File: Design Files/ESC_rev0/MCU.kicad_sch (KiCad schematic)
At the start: 35 parts, among them J1 Conn_01x08, J2 Conn_01x06, J3 Conn_01x03, SW1 Push Button, U4 STM32F405RGTx, Y1 Crystal

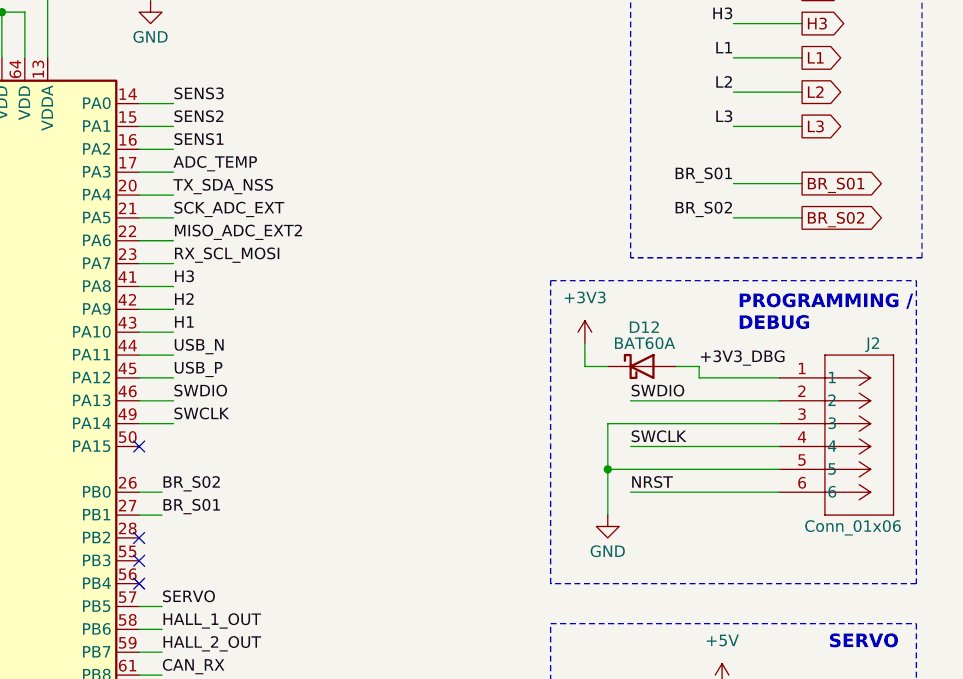
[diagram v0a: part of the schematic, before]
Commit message: update 18
Route process partially complete. Some corrections were made in footprints and pins references. Probably the power lines will need changes in size.
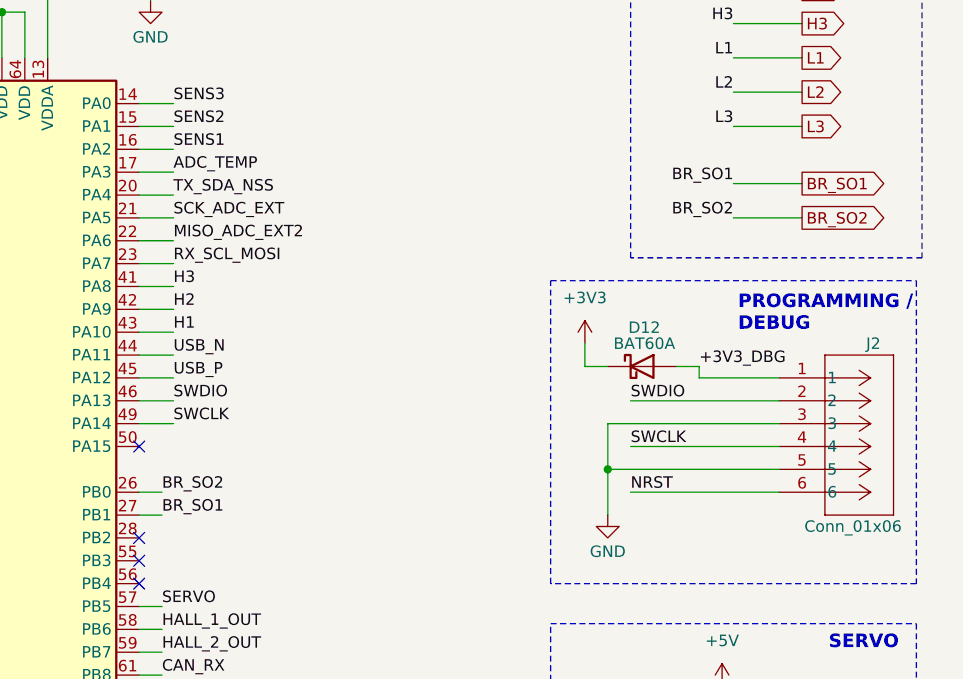
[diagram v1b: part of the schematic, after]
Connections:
- net BR_S01 renamed BR_SO1
- net BR_S02 renamed BR_SO2
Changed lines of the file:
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@@
 		)
 	)
-	(label "BR_S02"
+	(label "BR_SO2"
 		(at 182.88 115.57 0)
 		(fields_autoplaced yes)
@@
 		)
 	)
-	(label "BR_S01"
+	(label "BR_SO1"
 		(at 182.88 118.11 0)
 		(fields_autoplaced yes)
@@
 		)
 	)
-	(label "BR_S01"
+	(label "BR_SO1"
 		(at 246.38 81.28 180)
 		(fields_autoplaced yes)
@@
 		)
 	)
-	(label "BR_S02"
+	(label "BR_SO2"
 		(at 246.38 85.09 180)
 		(fields_autoplaced yes)
@@
 		)
 	)
-	(global_label "BR_S01"
+	(global_label "BR_SO1"
 		(shape output)
 		(at 254 81.28 0)
@@
 		)
 		(property "Intersheetrefs" "${INTERSHEET_REFS}"
-			(at 264.1213 81.28 0)
+			(at 264.2423 81.28 0)
 			(effects
 				(font
@@
 		)
 	)
-	(global_label "BR_S02"
+	(global_label "BR_SO2"
 		(shape output)
 		(at 254 85.09 0)
@@
 		)
 		(property "Intersheetrefs" "${INTERSHEET_REFS}"
-			(at 264.1213 85.09 0)
+			(at 264.2423 85.09 0)
 			(effects
 				(font
@@
 		(on_board yes)
 		(dnp no)
-		(fields_autoplaced yes)
 		(property "Reference" "FB1"
 			(at 191.7192 38.1 90)

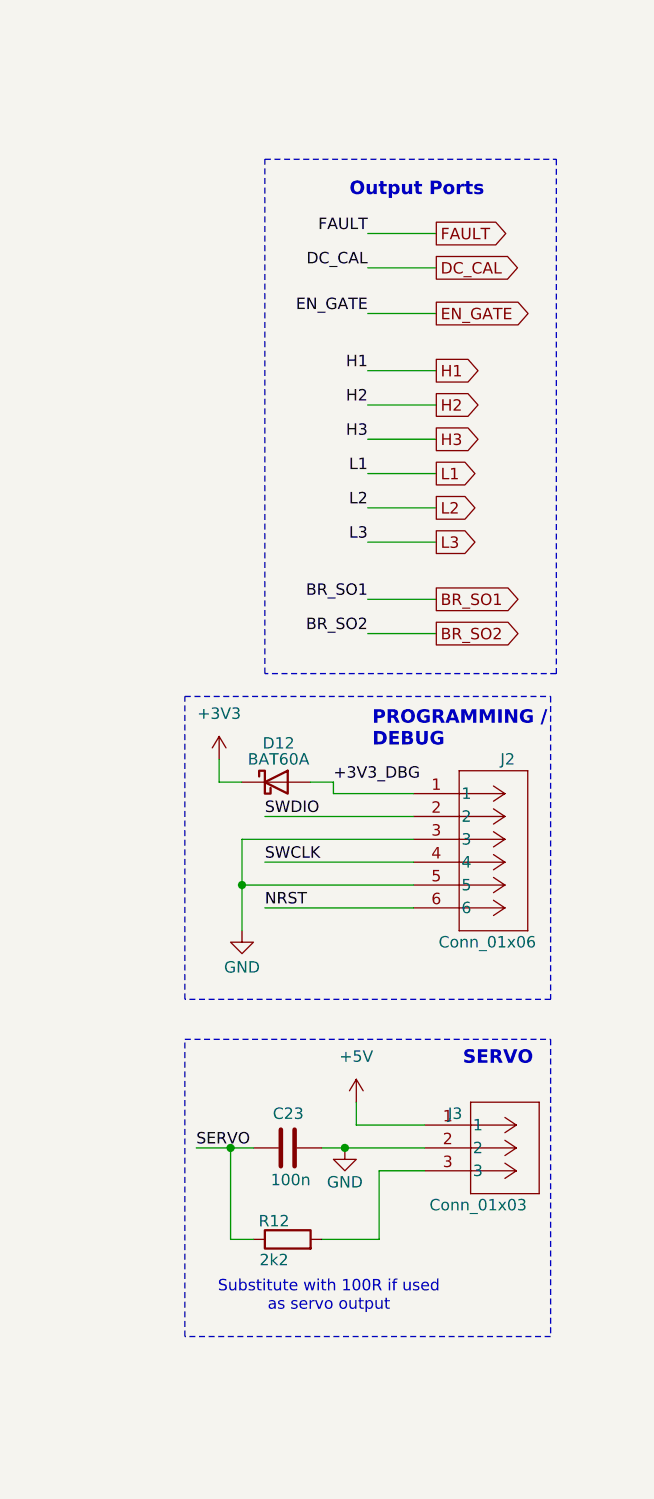
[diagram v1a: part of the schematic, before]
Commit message: update 19
Preliminary routing finished, all signaling connections made.
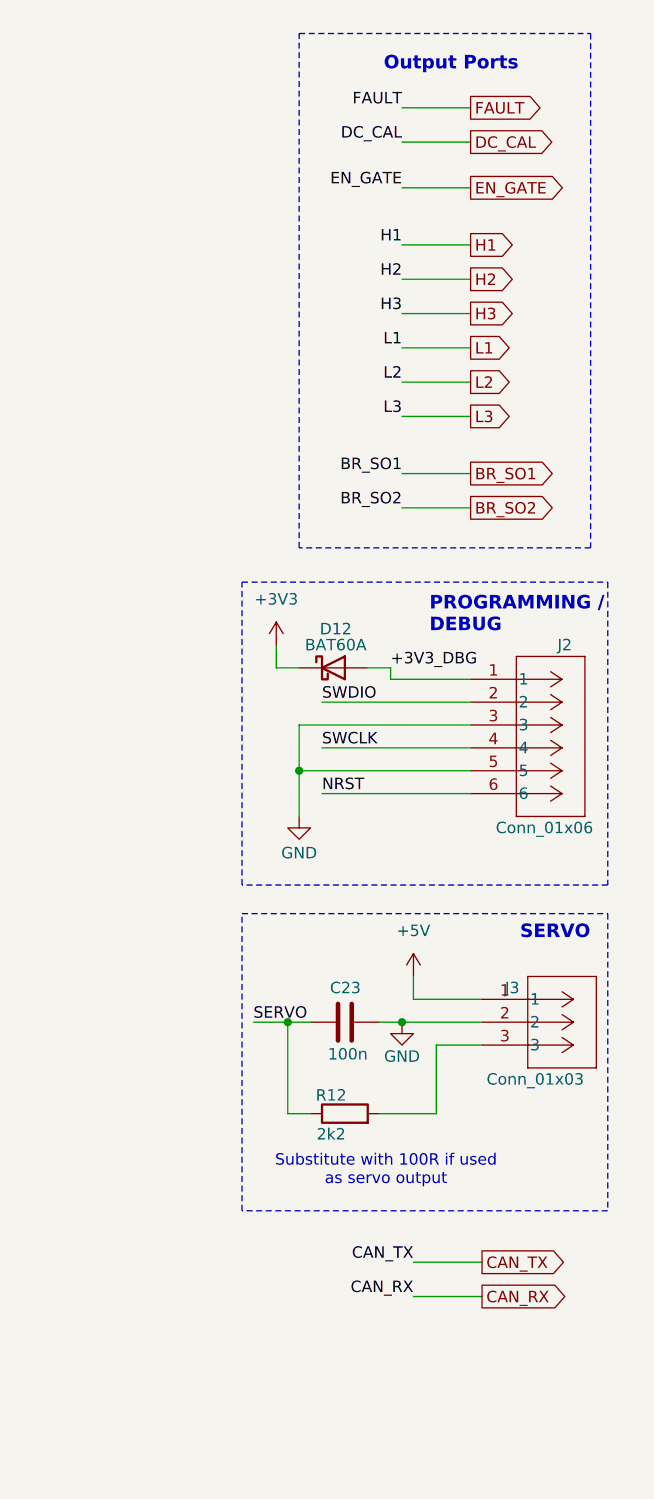
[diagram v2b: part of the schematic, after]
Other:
- moved on the sheet: C23, D12, J2, J3, R12
